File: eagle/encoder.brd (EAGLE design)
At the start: 100 x 80 mm, 19 parts, among them IC1 LM339D, J1 SPI, U1 MCP42XXX, U2 ATMEGA328P

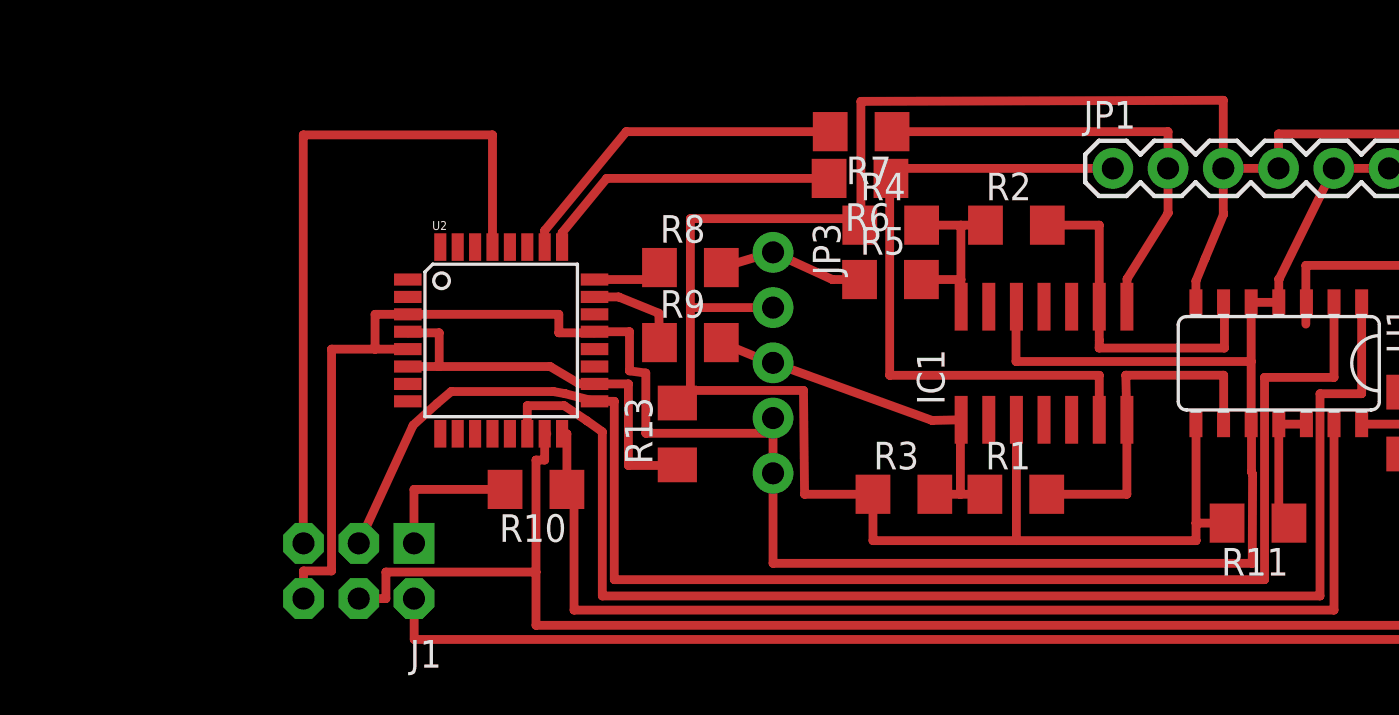
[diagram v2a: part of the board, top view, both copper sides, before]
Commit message: Added crystal.
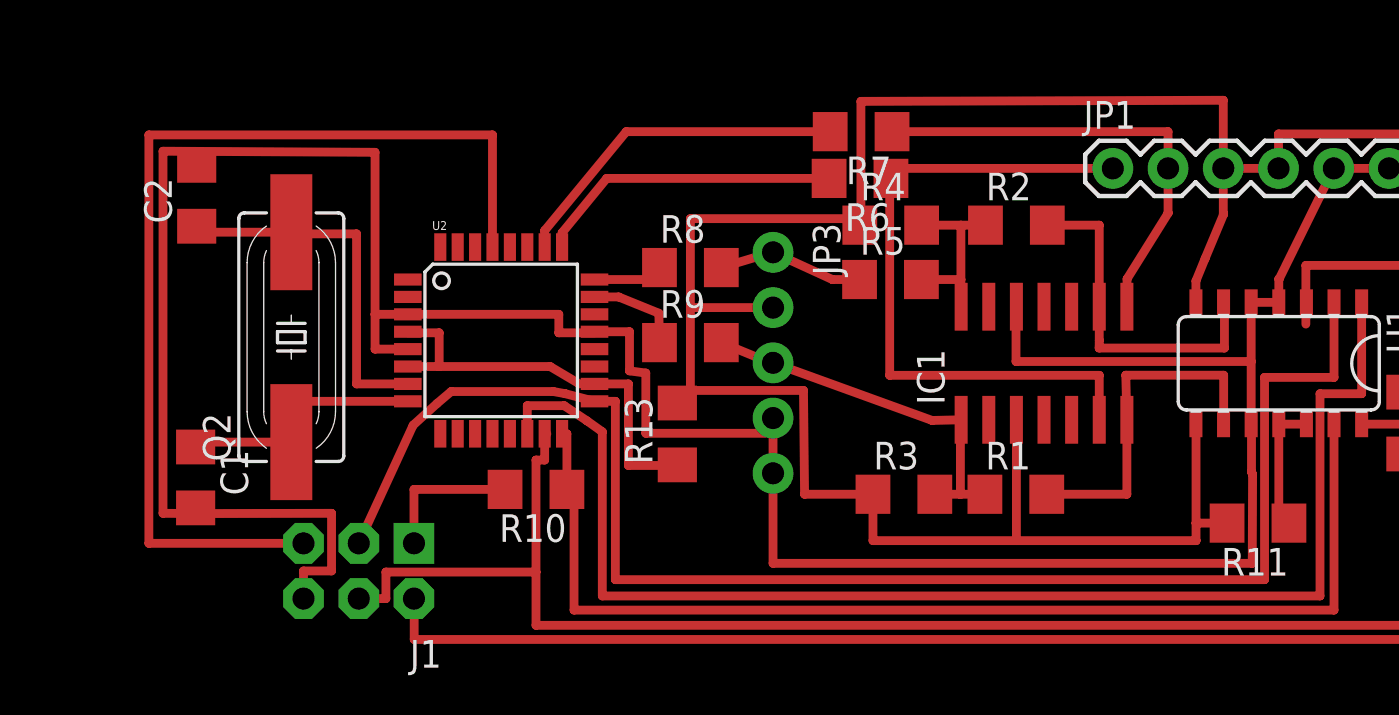
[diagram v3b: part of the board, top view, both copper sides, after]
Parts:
- added C1, C2: (no value), resistor:C1206
- added Q2: (no value), crystal:HC49UP
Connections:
- new net N$10: C1.1, Q2.1, U2.8
- new net N$11: C2.1, Q2.2, U2.7
- net GND: now also C1.2, C2.2
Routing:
- net GND: track 106.3 -> 139.5 mm
- net N$11: track 0.00 -> 17.0 mm
- net RESET: track 32.6 -> 46.8 mm
- net N$10: track 0.00 -> 11.9 mm
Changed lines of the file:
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@@
 <element name="R12" library="resistor" package="R1206" value="0" x="93.2" y="46.45" rot="R270"/>
 <element name="R13" library="resistor" package="R1206" value="0" x="59.7" y="45.95" rot="R90"/>
+<element name="Q2" library="crystal" package="HC49UP" value="" x="41.95" y="50.4" rot="R90">
+<attribute name="OC_NEWARK" value="unknown" x="41.95" y="50.4" size="1.778" layer="27" rot="R90" display="off"/>
+<attribute name="MPN" value="" x="41.95" y="50.4" size="1.778" layer="27" rot="R90" display="off"/>
+<attribute name="MF" value="" x="41.95" y="50.4" size="1.778" layer="27" rot="R90" display="off"/>
+<attribute name="OC_FARNELL" value="unknown" x="41.95" y="50.4" size="1.778" layer="27" rot="R90" display="off"/>
+</element>
+<element name="C1" library="resistor" package="C1206" value="" x="37.55" y="43.95" rot="R270"/>
+<element name="C2" library="resistor" package="C1206" value="" x="37.6" y="56.9" rot="R90"/>
 </elements>
 <signals>
@@
 <contactref element="U2" pad="5"/>
 <wire x1="47.3074" y1="49.85" x2="45.8" y2="49.85" width="0.4064" layer="1"/>
-<wire x1="45.8" y1="49.85" x2="43.8" y2="49.85" width="0.4064" layer="1"/>
-<wire x1="43.8" y1="49.85" x2="43.8" y2="39.65" width="0.4064" layer="1"/>
 <wire x1="43.8" y1="39.65" x2="42.51" y2="39.65" width="0.4064" layer="1"/>
 <wire x1="42.51" y1="39.65" x2="42.51" y2="38.38" width="0.4064" layer="1"/>
@@
 <wire x1="57.5" y1="50.65" x2="55.8926" y2="50.65" width="0.4064" layer="1"/>
 <wire x1="58.25" y1="45.98" x2="64.1" y2="45.98" width="0.4064" layer="1"/>
+<contactref element="C1" pad="2"/>
+<contactref element="C2" pad="2"/>
+<wire x1="45.8" y1="51.45" x2="45.8" y2="58.9" width="0.4064" layer="1"/>
+<wire x1="45.8" y1="58.9" x2="37.653034375" y2="58.941778125" width="0.4064" layer="1"/>
+<wire x1="37.653034375" y1="58.941778125" x2="36.05" y2="58.95" width="0.4064" layer="1"/>
+<wire x1="36.05" y1="58.95" x2="36.05" y2="42.3" width="0.4064" layer="1"/>
+<wire x1="36.05" y1="42.3" x2="37.6989625" y2="42.2893625" width="0.4064" layer="1"/>
+<wire x1="37.6989625" y1="42.2893625" x2="43.8" y2="42.3" width="0.4064" layer="1"/>
+<wire x1="43.8" y1="42.3" x2="43.8" y2="39.65" width="0.4064" layer="1"/>
+<wire x1="37.6" y1="58.3" x2="37.653034375" y2="58.3" width="0.4064" layer="1"/>
+<wire x1="37.653034375" y1="58.3" x2="37.653034375" y2="58.941778125" width="0.4064" layer="1"/>
+<wire x1="37.55" y1="42.55" x2="37.6989625" y2="42.55" width="0.4064" layer="1"/>
+<wire x1="37.6989625" y1="42.55" x2="37.6989625" y2="42.2893625" width="0.4064" layer="1"/>
 </signal>
 <signal name="N$5">
@@
 <contactref element="U1" pad="2"/>
 <contactref element="J1" pad="3"/>
-<wire x1="55.8926" y1="47.45" x2="56.8" y2="47.45" width="0.4064" layer="1"/>
-<wire x1="56.8" y1="47.45" x2="56.8" y2="39.25" width="0.4064" layer="1"/>
-<wire x1="56.8" y1="39.25" x2="86.7" y2="39.25" width="0.4064" layer="1"/>
+<wire x1="55.8926" y1="47.45" x2="56.85" y2="47.45" width="0.4064" layer="1"/>
+<wire x1="56.85" y1="47.45" x2="56.85" y2="39.25" width="0.4064" layer="1"/>
+<wire x1="56.85" y1="39.25" x2="86.7" y2="39.25" width="0.4064" layer="1"/>
 <wire x1="45.05" y1="40.92" x2="47.55" y2="46.35" width="0.4064" layer="1"/>
 <wire x1="47.55" y1="46.35" x2="48.65" y2="47.35" width="0.4064" layer="1"/>
@@
 <wire x1="51.2" y1="54.5426" x2="51.2" y2="59.7" width="0.4064" layer="1"/>
 <contactref element="J1" pad="5"/>
-<wire x1="42.51" y1="40.92" x2="42.5" y2="40.92" width="0.4064" layer="1"/>
-<wire x1="42.5" y1="40.92" x2="42.5" y2="59.7" width="0.4064" layer="1"/>
-<wire x1="42.5" y1="59.7" x2="51.2" y2="59.7" width="0.4064" layer="1"/>
+<wire x1="42.51" y1="40.92" x2="35.4" y2="40.92" width="0.4064" layer="1"/>
+<wire x1="35.4" y1="40.92" x2="35.4" y2="59.7" width="0.4064" layer="1"/>
+<wire x1="35.4" y1="59.7" x2="51.2" y2="59.7" width="0.4064" layer="1"/>
 </signal>
 <signal name="SS">
@@
 <wire x1="55.2" y1="48.25" x2="55.8926" y2="48.25" width="0" layer="19" extent="1-1"/>
 </signal>
+<signal name="N$10">
+<contactref element="U2" pad="8"/>
+<contactref element="Q2" pad="1"/>
+<contactref element="C1" pad="1"/>
+<wire x1="47.3074" y1="47.45" x2="41.95" y2="47.45" width="0.4064" layer="1"/>
+<wire x1="41.95" y1="47.45" x2="41.95" y2="45.574" width="0.4064" layer="1"/>
+<wire x1="41.95" y1="45.574" x2="37.55" y2="45.574" width="0.4064" layer="1"/>
+<wire x1="37.55" y1="45.574" x2="37.55" y2="45.35" width="0.4064" layer="1"/>
+</signal>
+<signal name="N$11">
+<contactref element="U2" pad="7"/>
+<contactref element="Q2" pad="2"/>
+<contactref element="C2" pad="1"/>
+<wire x1="47.3074" y1="48.25" x2="44.95" y2="48.25" width="0.4064" layer="1"/>
+<wire x1="44.95" y1="48.25" x2="44.95" y2="55.15" width="0.4064" layer="1"/>
+<wire x1="44.95" y1="55.15" x2="41.95" y2="55.15" width="0.4064" layer="1"/>
+<wire x1="41.95" y1="55.15" x2="41.95" y2="55.226" width="0.4064" layer="1"/>
+<wire x1="41.95" y1="55.226" x2="37.6" y2="55.226" width="0.4064" layer="1"/>
+<wire x1="37.6" y1="55.226" x2="37.6" y2="55.5" width="0.4064" layer="1"/>
+</signal>
 </signals>
